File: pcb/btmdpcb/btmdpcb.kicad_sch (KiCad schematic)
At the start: 56 parts, among them J1 USB_C_Receptacle_PowerOnly_6P, J2 ANT, Q1 AO3401A, Q2 AO3401A, Q3 MMBT3904, T1 ED8_4, T2 ED8_4, U2 ME6211C33M5, U3 AMS1117-1.5, U4 TP4057, U5 MC34063AD

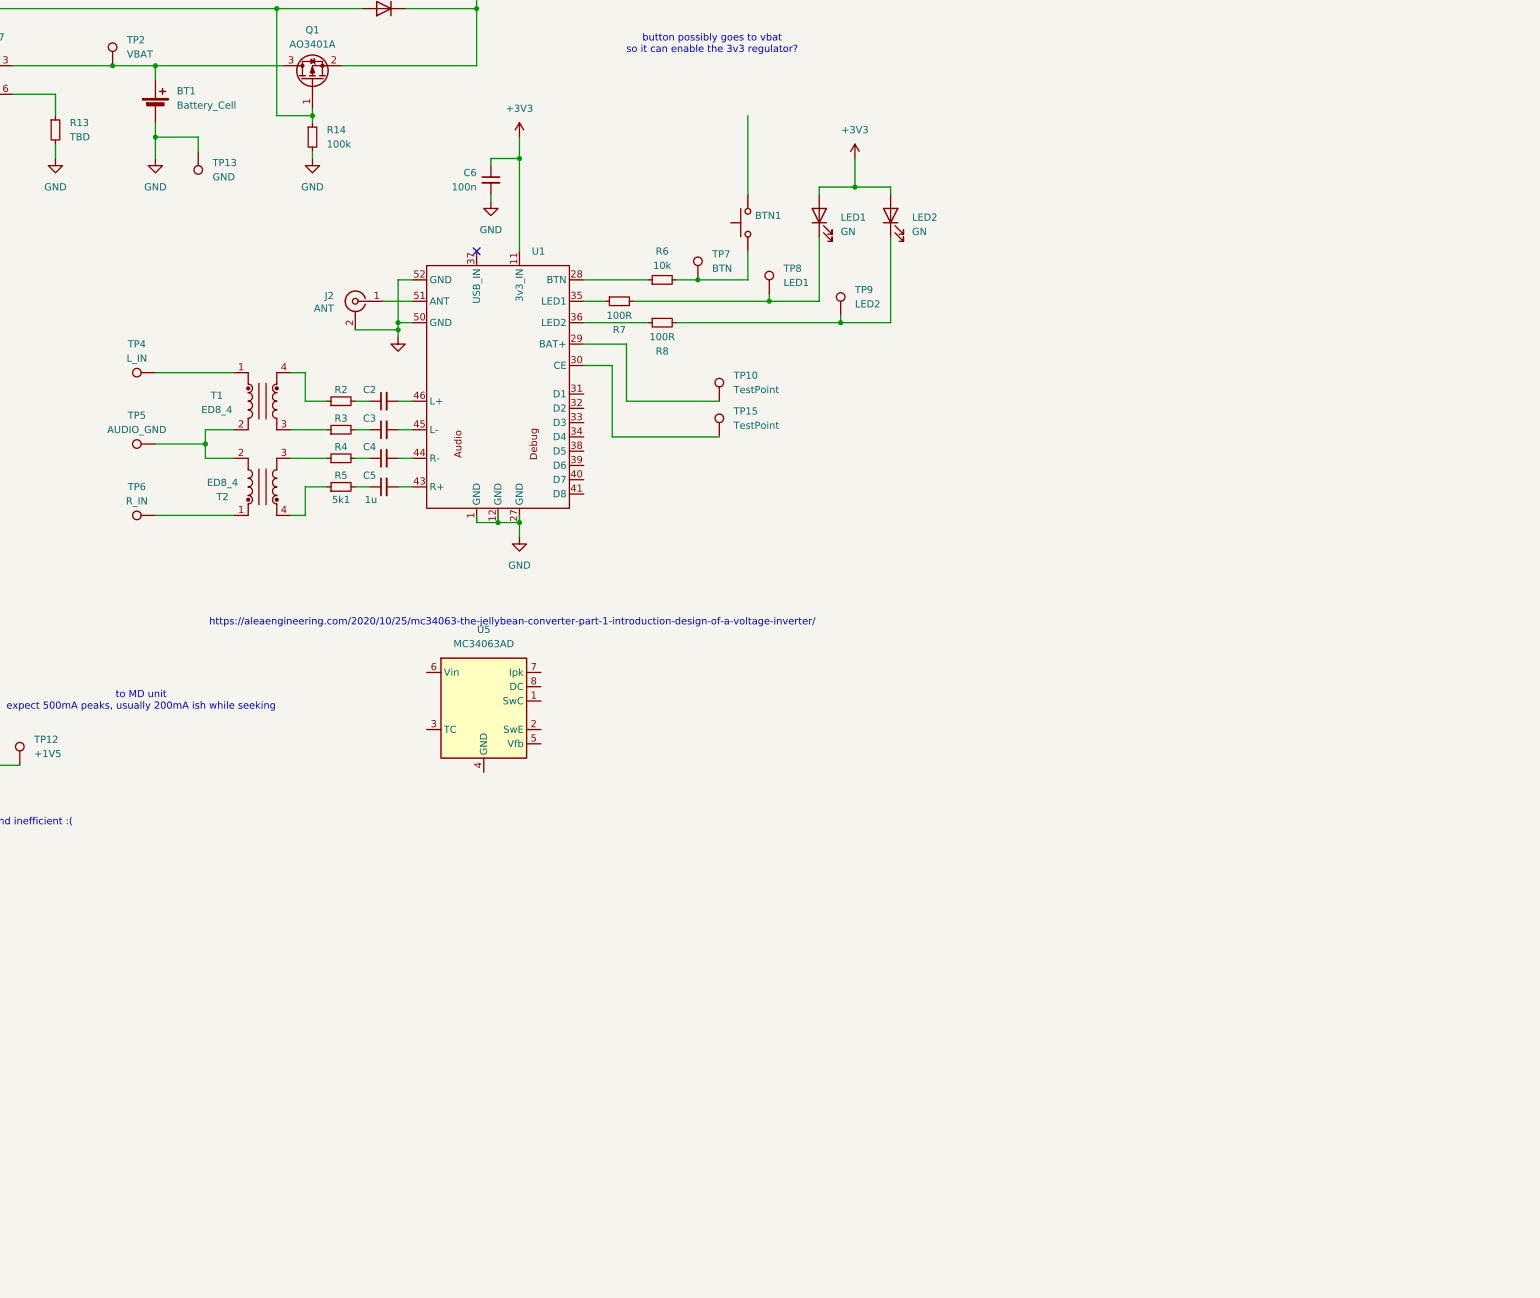
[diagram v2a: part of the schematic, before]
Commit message: Separate BT and Pololu libraries
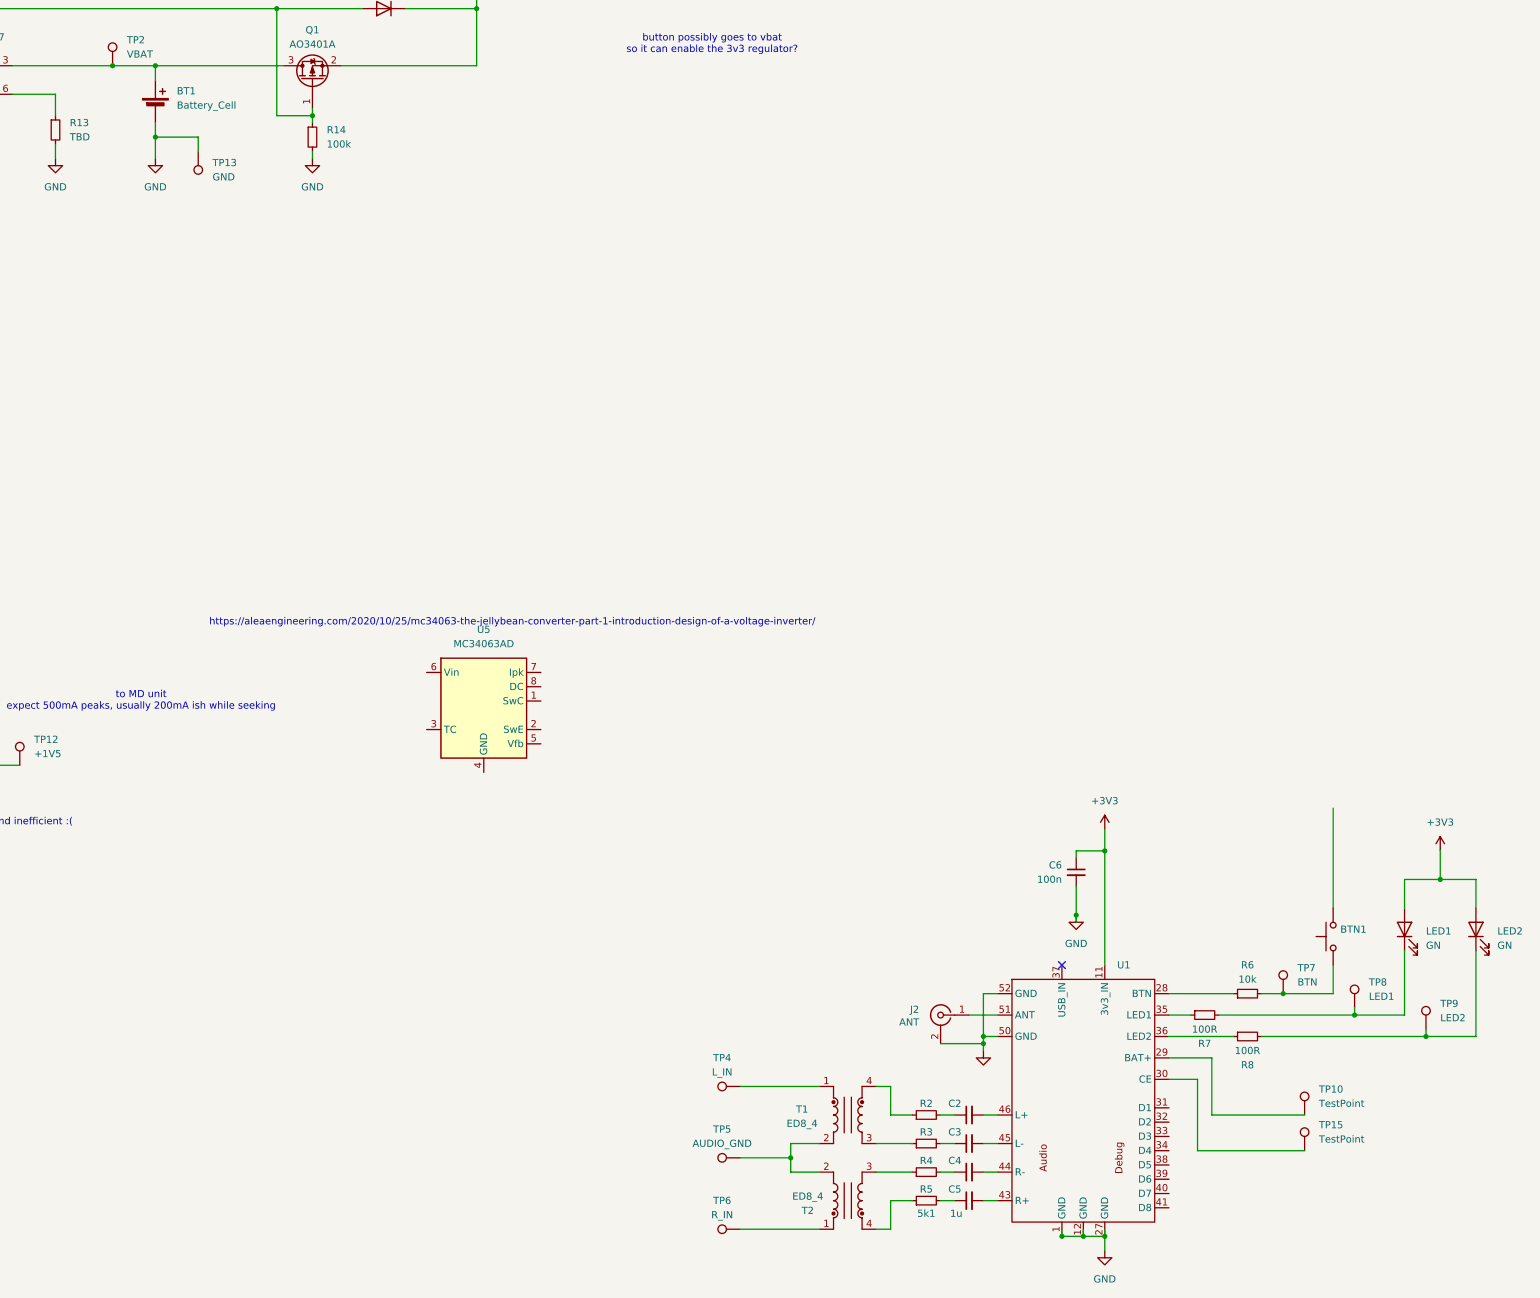
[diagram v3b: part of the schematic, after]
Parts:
- U1: footprint modules:BT -> bt_audio:bt_audio_smd; symbol modules:BTmod -> bt_audio:Scosche_FlyTunes_BT_audio_module
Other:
- title: (none) -> BTMD: Bluetooth Minidisc
- moved on the sheet: BTN1, C2, C3, C4, C5, C6, J2, LED1, LED2, R2, R3, R4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

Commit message: [WIP] Design eval board for all relevant functions
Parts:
- removed BT1: Battery_Cell, symbol Device:Battery_Cell
- removed BTN1: SW_Push, symbol Switch:SW_Push
- removed C2, C3, C4, C5: 1u, Capacitor_SMD:C_0603_1608Metric_Pad1.08x0.95mm_HandSolder, symbol Device:C_Small
- removed C6: 100n, Capacitor_SMD:C_0603_1608Metric_Pad1.08x0.95mm_HandSolder, symbol Device:C_Small
- removed D1: GS1A, symbol Device:D
- removed J1: USB_C_Receptacle_PowerOnly_6P, symbol Connector:USB_C_Receptacle_PowerOnly_6P
- removed J2: ANT, Connector_Coaxial:U.FL_Molex_MCRF_73412-0110_Vertical, symbol Connector:Conn_Coaxial
- removed LED1, LED2, LED4: GN, LED_SMD:LED_0603_1608Metric_Pad1.05x0.95mm_HandSolder, symbol Device:LED
- removed LED3: RD, LED_SMD:LED_0603_1608Metric_Pad1.05x0.95mm_HandSolder, symbol Device:LED
- removed Q1, Q2: AO3401A, Package_TO_SOT_SMD:SOT-23, symbol Transistor_FET:AO3401A
- removed Q3: MMBT3904, Package_TO_SOT_SMD:SOT-23, symbol Transistor_BJT:MMBT3904
- removed R1, R10: 5k1, symbol Device:R_Small
- removed R11, R12: 330R, symbol Device:R_Small
- removed R13: TBD, symbol Device:R_Small
- removed R14: 100k, symbol Device:R_Small
- removed R17: 0R, symbol Device:R_Small
- removed R2, R3, R4, R5: 5k1, Resistor_SMD:R_0603_1608Metric_Pad0.98x0.95mm_HandSolder, symbol Device:R_Small
- removed R6: 10k, Resistor_SMD:R_0603_1608Metric_Pad0.98x0.95mm_HandSolder, symbol Device:R_Small
- removed R7, R8: 100R, Resistor_SMD:R_0603_1608Metric_Pad0.98x0.95mm_HandSolder, symbol Device:R_Small
- removed T1, T2: ED8_4, Transformer_SMD:Transformer_ED8_4-Lead_10.5x8mm_P5mm, symbol Transformer:ED8_4
- removed TP1: VUSB, symbol Connector:TestPoint
- removed TP10, TP15: TestPoint, TestPoint:TestPoint_Pad_D1.0mm, symbol Connector:TestPoint
- removed TP11: +3V3, symbol Connector:TestPoint
- removed TP12: +1V5, symbol Connector:TestPoint
- removed TP13: GND, symbol Connector:TestPoint
- removed TP14: CE, symbol Connector:TestPoint
- removed TP2: VBAT, symbol Connector:TestPoint
- removed TP3: VCC, symbol Connector:TestPoint
- removed TP4: L_IN, TestPoint:TestPoint_Pad_D1.0mm, symbol Connector:TestPoint
- removed TP5: AUDIO_GND, TestPoint:TestPoint_Pad_D1.0mm, symbol Connector:TestPoint
- removed TP6: R_IN, TestPoint:TestPoint_Pad_D1.0mm, symbol Connector:TestPoint
- removed TP7: BTN, TestPoint:TestPoint_Pad_D1.0mm, symbol Connector:TestPoint
- removed TP8: LED1, TestPoint:TestPoint_Pad_D1.0mm, symbol Connector:TestPoint
- removed TP9: LED2, TestPoint:TestPoint_Pad_D1.0mm, symbol Connector:TestPoint
- removed U1: ~, bt_audio:bt_audio_smd, symbol bt_audio:Scosche_FlyTunes_BT_audio_module
- removed U2: ME6211C33M5, Package_TO_SOT_SMD:SOT-23-5, symbol Regulator_Linear:ME6211C33M5
- removed U3: AMS1117-1.5, Package_TO_SOT_SMD:SOT-223-3_TabPin2, symbol Regulator_Linear:AMS1117-1.5
- removed U4: TP4057, Package_TO_SOT_SMD:TSOT-23-5, symbol Battery_Management:TP4057
- removed U5: MC34063AD, Package_SO:SOIC-8_3.9x4.9mm_P1.27mm, symbol Regulator_Switching:MC34063AD
- added C11: C, symbol Device:C
- added C12, C13, C14: 100n, symbol Device:C
- added C15: 1u or more, symbol Device:C
- added D3, D4, D5: LED, symbol Device:LED
- added JP1, JP2, JP3, JP4, JP5, JP7, JP8: Jumper_2_Bridged, symbol Jumper:Jumper_2_Bridged
- added JP6: Jumper_3_Bridged12, symbol Jumper:Jumper_3_Bridged12
- added Q4, Q5: AO3401A, Package_TO_SOT_SMD:SOT-23, symbol Transistor_FET:AO3401A
- added Q6, Q8: BSD235C, Package_TO_SOT_SMD:SOT-363_SC-70-6, symbol Transistor_FET:BSD235C
- added R22: R, symbol Device:R
- added R23: 1k, symbol Device:R
- added R24, R25: 100k, symbol Device:R
- added R26: 0, symbol Device:R_Small
- added R27: 10k, symbol Device:R
- added R28: 100k, symbol Device:R_Small
- added R39, R40, R41: 220R, symbol Device:R
- added SW_BT1: SW_Push, symbol Switch:SW_Push
- R15: value 10k -> 100R
- R16: value 100k -> 10k
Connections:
- net +1V5: now also Q8.2 (GN), R22.2
- net +3V3: now also C12.1, C15.1, D4.2 (A), Q5.2 (S), R24.2, SW_BT1.1
- net GND: now also C11.2, C12.2, C13.2, C14.2, C15.2, JP6.3 (B), Q6.1 (SN), Q8.1 (SN), R27.2, R28.2, R39.2, R40.2
- net +2V5: now reaches R15.1
- net +2V5: now also C13.1
- net at R15.2, R16.1: now also Q6.2 (GN)
- net ~{EN_1V5}: now reaches R9.2
- net ~{EN_1V5}: now also Q4.1 (G), Q6.5 (GP), Q6.6 (DN), R25.1, R26.2
- net VCC renamed +BATT
- net +BATT: now also D5.2 (A), JP1.1 (A), JP2.1 (A), JP3.1 (A), JP7.1 (A), Q6.4 (SP)
- new net: D5.1 (K), R41.1
- new net: Q8.6 (DN), R41.2
- new net: D4.1 (K), R40.1
- new net: JP1.2 (B), JP8.1 (A), Q4.2 (S), R25.2
- new net: Q5.3 (D), R23.1, SW_BT1.2
- new net: D3.1 (K), R39.1
- new net EN_1V5: JP4.2 (B), JP5.2 (B), Q6.3 (DP), R28.1
- new net MD unit (MZ-N505)/~{BTN_PAUSE}_OUT: R26.1
- new net MD unit (MZ-N505)/~{BTN_REC}_OUT: Q5.1 (G), R24.1
- new net bt_module/BTN: C14.1, D3.2 (A), R23.2, R27.1
- new net power_3v3/EN: C11.1, R22.1
- new net power_3v3/Vin: JP7.2 (B)
- new net power_ap3xxx/Vin: JP2.2 (B), JP4.1 (A)
- new net power_mc34063/Vin: JP8.2 (B), Q4.3 (D)
- new net power_we/MODE: JP6.2 (C)
- new net power_we/Vin: JP3.2 (B), JP5.1 (A), JP6.1 (A)
- no-connect marks 1 -> 6
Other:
- added sheet MD unit (MZ-N505) (md_unit.kicad_sch)
- added sheet bt_module (bt_module.kicad_sch)
- added sheet dual_mosfet_hold (dual_mosfet.kicad_sch)
- added sheet dual_mosfet_hold_bt (dual_mosfet.kicad_sch)
- added sheet dual_mosfet_pause (dual_mosfet.kicad_sch)
- added sheet power_3v3 (power_3v3.kicad_sch)
- added sheet power_ap3xxx (power_ap3xxx.kicad_sch)
- added sheet power_mc34063 (power_mc34063.kicad_sch)
- added sheet power_we (power_we.kicad_sch)
- added sheet supply (supply.kicad_sch)
- note added: "bootstrap 1V5 regulator by pressing PAUSE key"
- note removed: "from bt module charge enable pin"
- note removed: "high-side switch, active high"
- note removed: "https://aleaengineering.com/2020/10/25/mc34063-the-jellybean-converter-part-1-introduction-design-of-a-voltage-inverter/"
- note removed: "to MD unit expect 500mA peaks, usually 200mA ish while seeking"
- note removed: "yes it's linear and inefficient :("
- moved on the sheet: R15, R16, R9
